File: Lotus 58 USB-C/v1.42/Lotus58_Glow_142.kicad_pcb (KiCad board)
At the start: 2 copper layers, 139.1 x 107.7 mm, 152 parts, among them J1 USB_C_Receptacle_USB2.0, P1 OLED, SW1 Kailh hotswap MX socket, SW10 Kailh hotswap MX socket, SW11 Kailh hotswap MX socket, SW12 Kailh hotswap MX socket, SW13 Kailh hotswap MX socket, SW14 Kailh hotswap MX socket, SW15 Kailh hotswap MX socket, SW16 Kailh hotswap MX socket, SW17 Kailh hotswap MX socket, SW18 Kailh hotswap MX socket, SW19 Kailh hotswap MX socket, SW2 Kailh hotswap MX socket, SW20 Kailh hotswap MX socket, SW21 Kailh hotswap MX socket, SW22 Kailh hotswap MX socket, SW23 Kailh hotswap MX socket, SW24 Kailh hotswap MX socket, SW25 Kailh hotswap MX socket, SW26 Kailh hotswap MX socket, SW27 Kailh hotswap MX socket, SW28 Kailh hotswap MX socket, SW29 Kailh hotswap MX socket, SW3 Kailh hotswap MX socket, SW30 Rotary_Encoder_Switch, SW31 Rotary_Encoder_Switch, SW32 MSK12C02, SW33 MSK12C02, SW4 Kailh hotswap MX socket, SW5 Kailh hotswap MX socket, SW6 Kailh hotswap MX socket, SW7 Kailh hotswap MX socket, SW8 Kailh hotswap MX socket, SW9 Kailh hotswap MX socket, U1 ProMicro, U2 SRV05-4, U3 SRV05-4

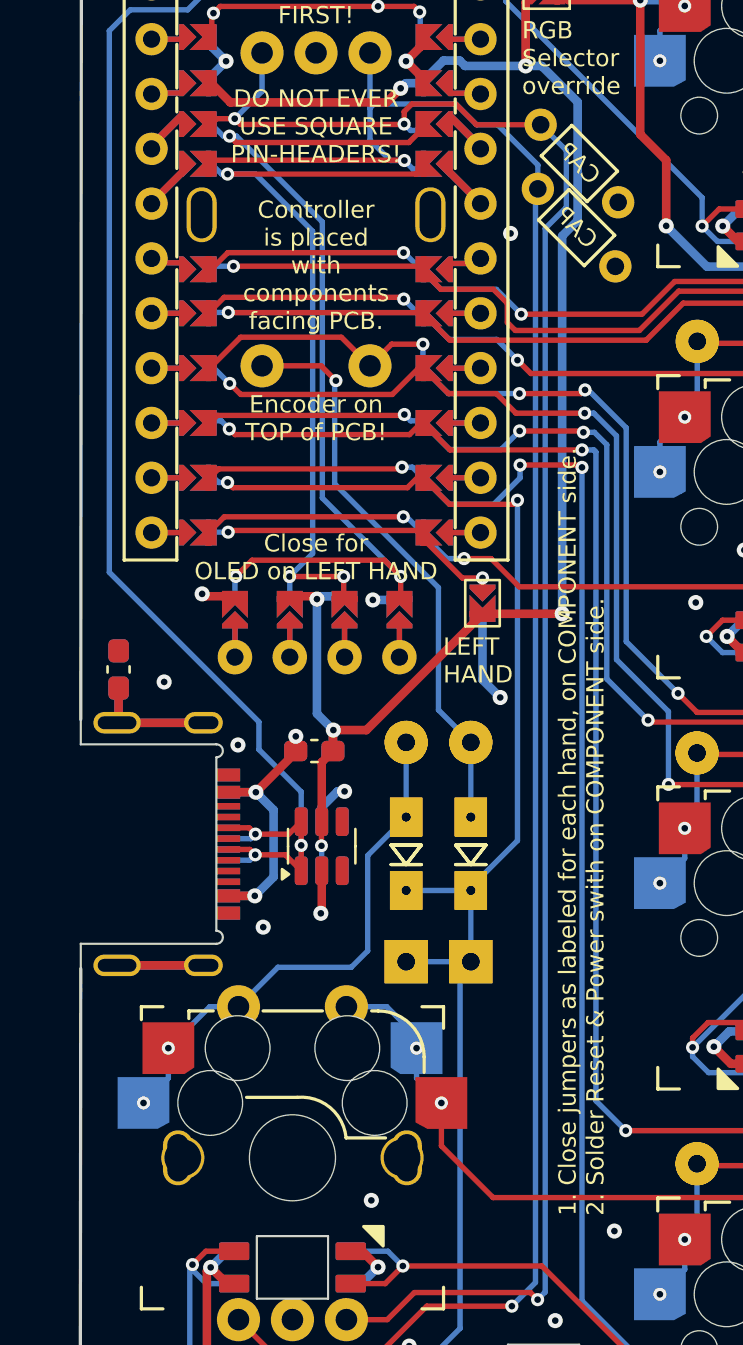
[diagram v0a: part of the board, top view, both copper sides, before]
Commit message: Lotus 58 - USB Link v1.51
adjusted RGB Gl
ow, Silkscreen

Signed-off-by: Markus Knutsson <markus.knutsson@tweety.se>
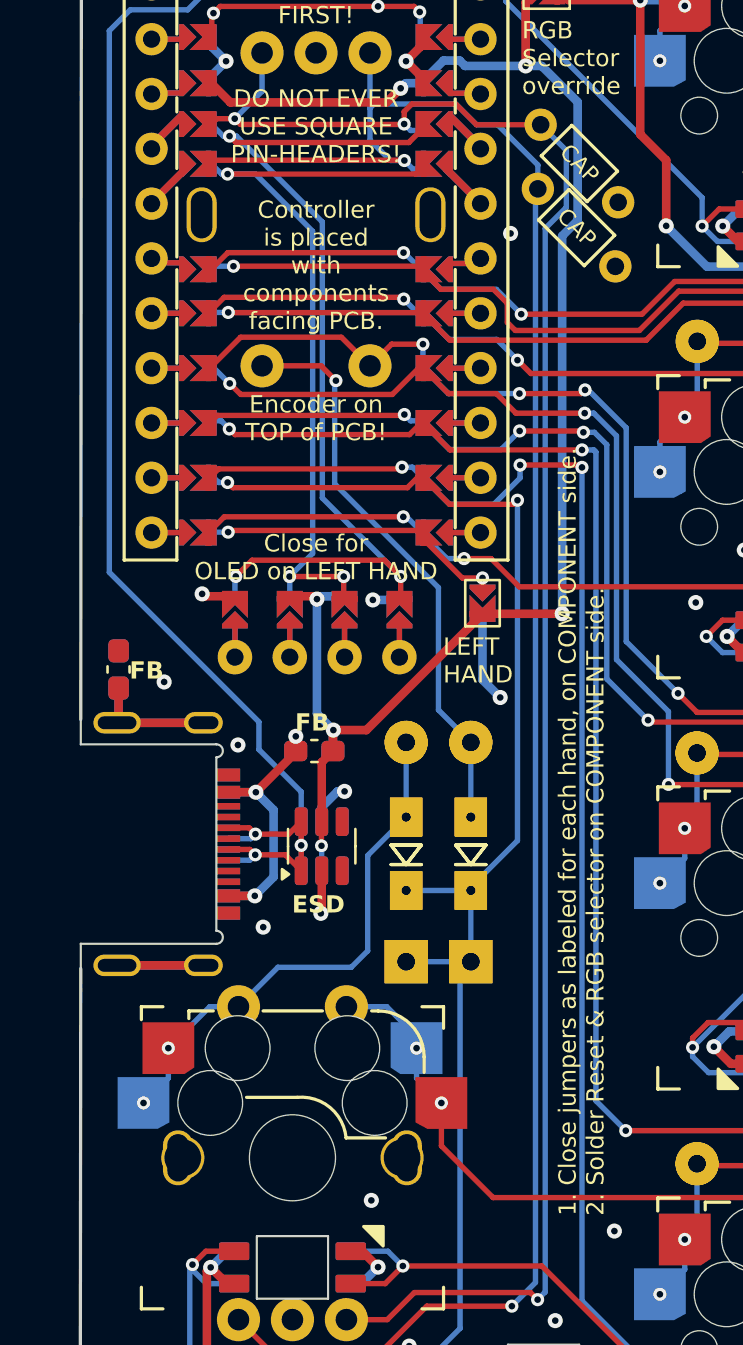
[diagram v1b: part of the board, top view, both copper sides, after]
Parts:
- turned C1 to 135 degrees
- renumbered FB3 to FB
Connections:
- C1 pad 1: EncB -> GND
- C1 pad 2: GND -> EncB
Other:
- board text added: "1. Close jumpers as labeled for each hand, on COMPONENT side. 2. Solder Reset & RGB selector on COMPONENT side."
- board text added: "ESD"
- board text added: "FB"
- board text added: "Use individual diode legs for controller/OLED, this makes removal/repair MUCH easier!"
- board text removed: "1. Close jumpers as labeled for each hand, on COMPONENT side. 2. Solder Reset & Power swith on COMPONENT side."
- board text removed: "Use individual diode legs for controller/OLED, this making removal/repair MUCH easier!"
